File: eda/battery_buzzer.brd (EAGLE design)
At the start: 47 x 26.7 mm, 30 parts, among them Q2 IRFML8244, U1 ISL83491SOIC, U2 ATTINY1634

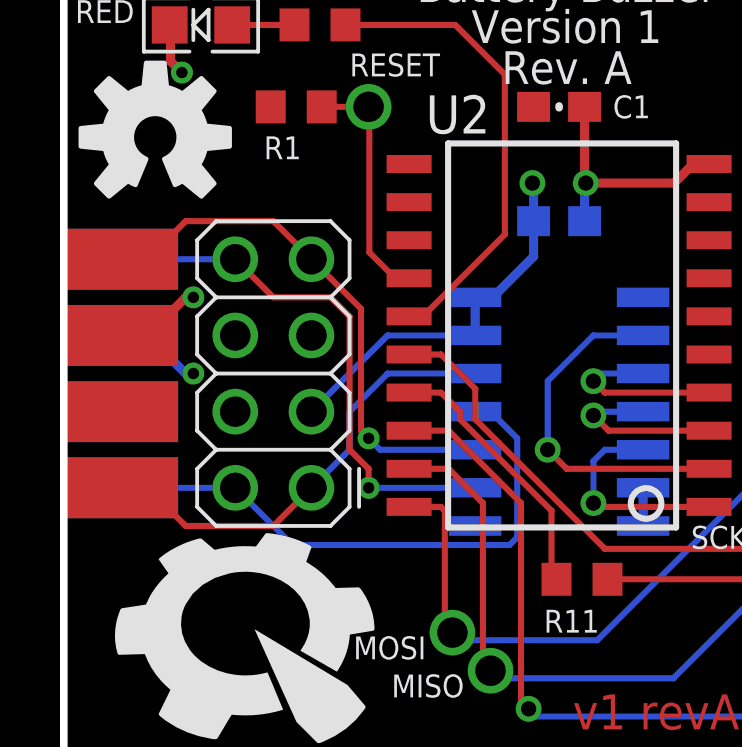
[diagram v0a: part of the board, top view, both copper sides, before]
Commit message: Change smartsensor connectors to 2x5
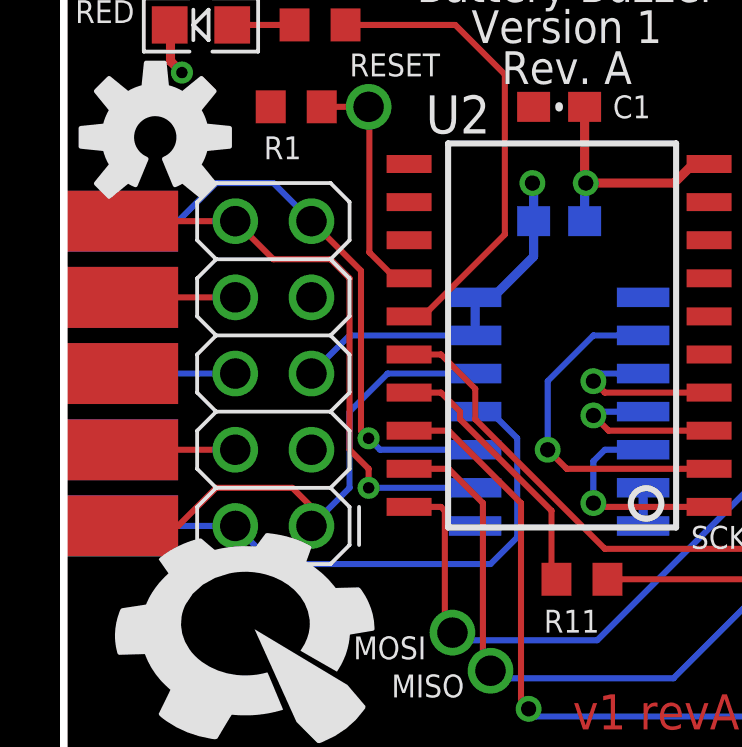
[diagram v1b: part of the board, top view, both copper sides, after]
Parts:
- U$14: value SENSOR_CONPTH -> (none); device pie:2X4 -> pie:2X5
- U$15: value SENSOR_CONSMD-EDGE -> (none); device pie:2X4-EDGE -> pie:2X5-EDGE
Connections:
- net 5V: now also U$14.5, U$15.5; no longer U$14.3, U$15.3
- net B_N: now also U$14.9, U$15.9; no longer U$14.7, U$15.7
- net B_P: now also U$14.10, U$15.10; no longer U$14.8, U$15.8
- net GND: now also U$14.3, U$14.7, U$14.8, U$15.3, U$15.7, U$15.8; no longer U$14.5, U$15.5
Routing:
- net GND: track 36.6 -> 41.2 mm, vias 6 -> 5
- net A_P: track 15.2 -> 19.3 mm
- net B_N: track 17.9 -> 19.1 mm
- net B_P: track 17.9 -> 19.2 mm
- net A_N: track 19.2 -> 18.7 mm
- net 5V: track 25.3 -> 25.7 mm, vias 2 -> 1
